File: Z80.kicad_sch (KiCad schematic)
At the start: 14 parts, among them J13 Conn_02x06_Odd_Even, J14 Conn_02x20_Odd_Even, J15 Conn_01x03_Socket, J16 Conn_01x03_Pin, SW3 RotaryEncoder_for_Coleco_20imp, U4 Z80CPU

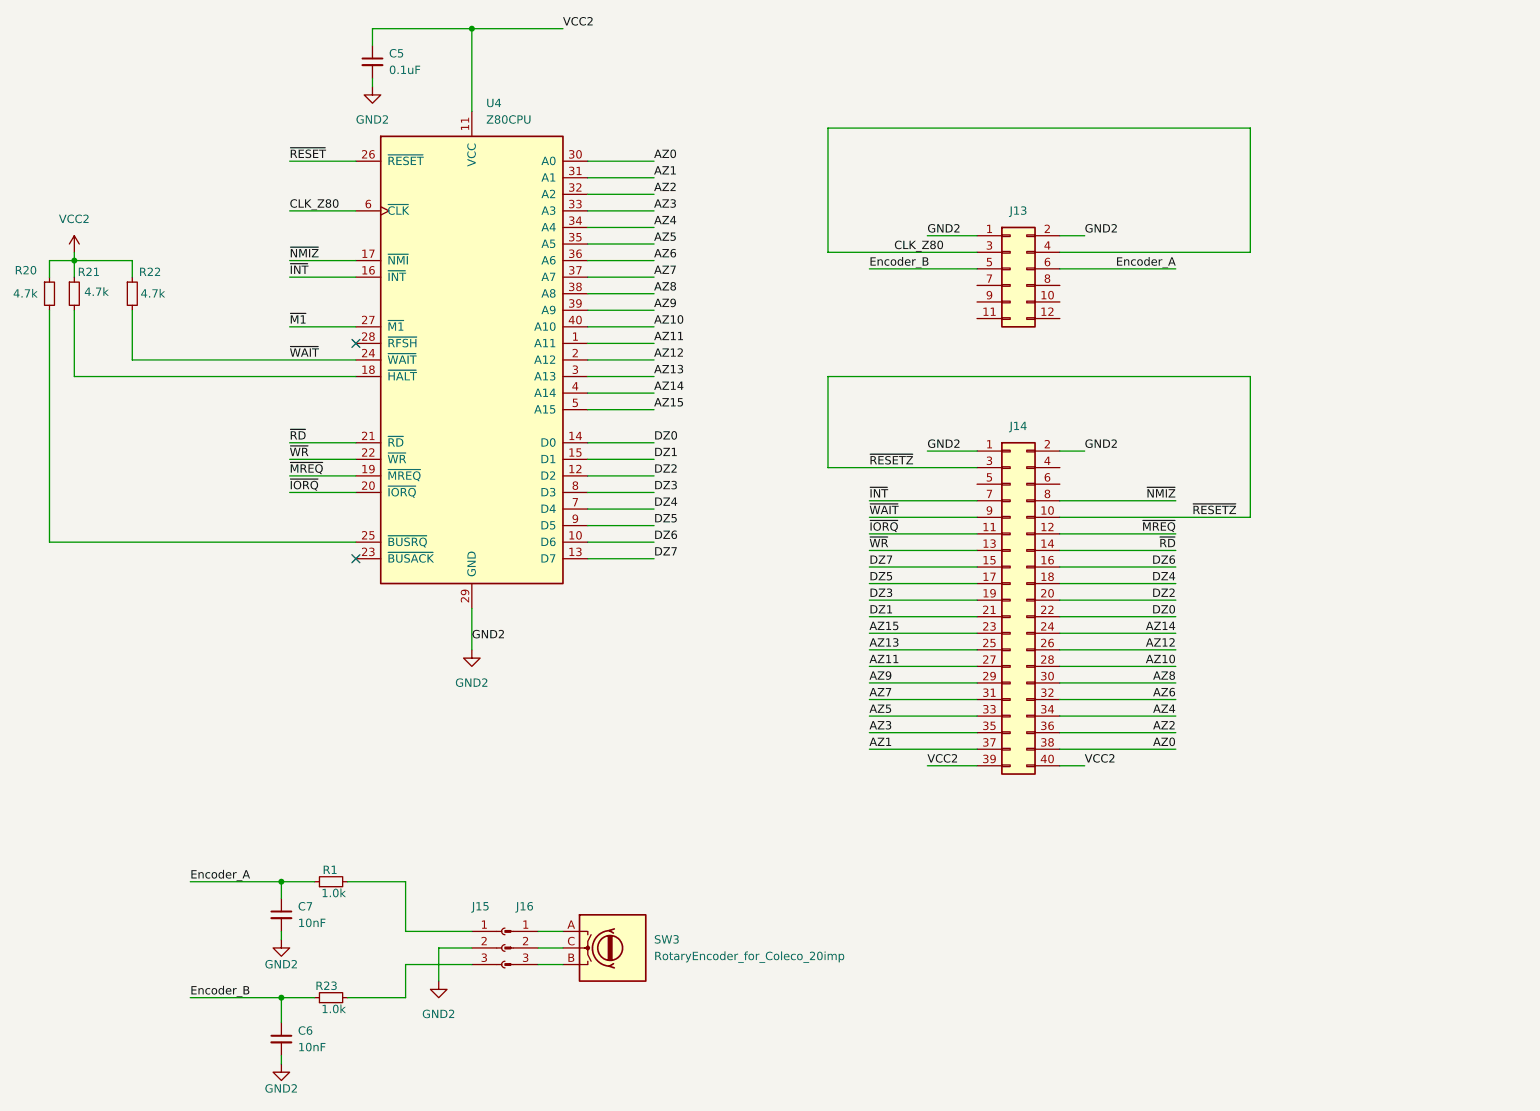
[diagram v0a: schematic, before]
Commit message: Update Z80.kicad_sch
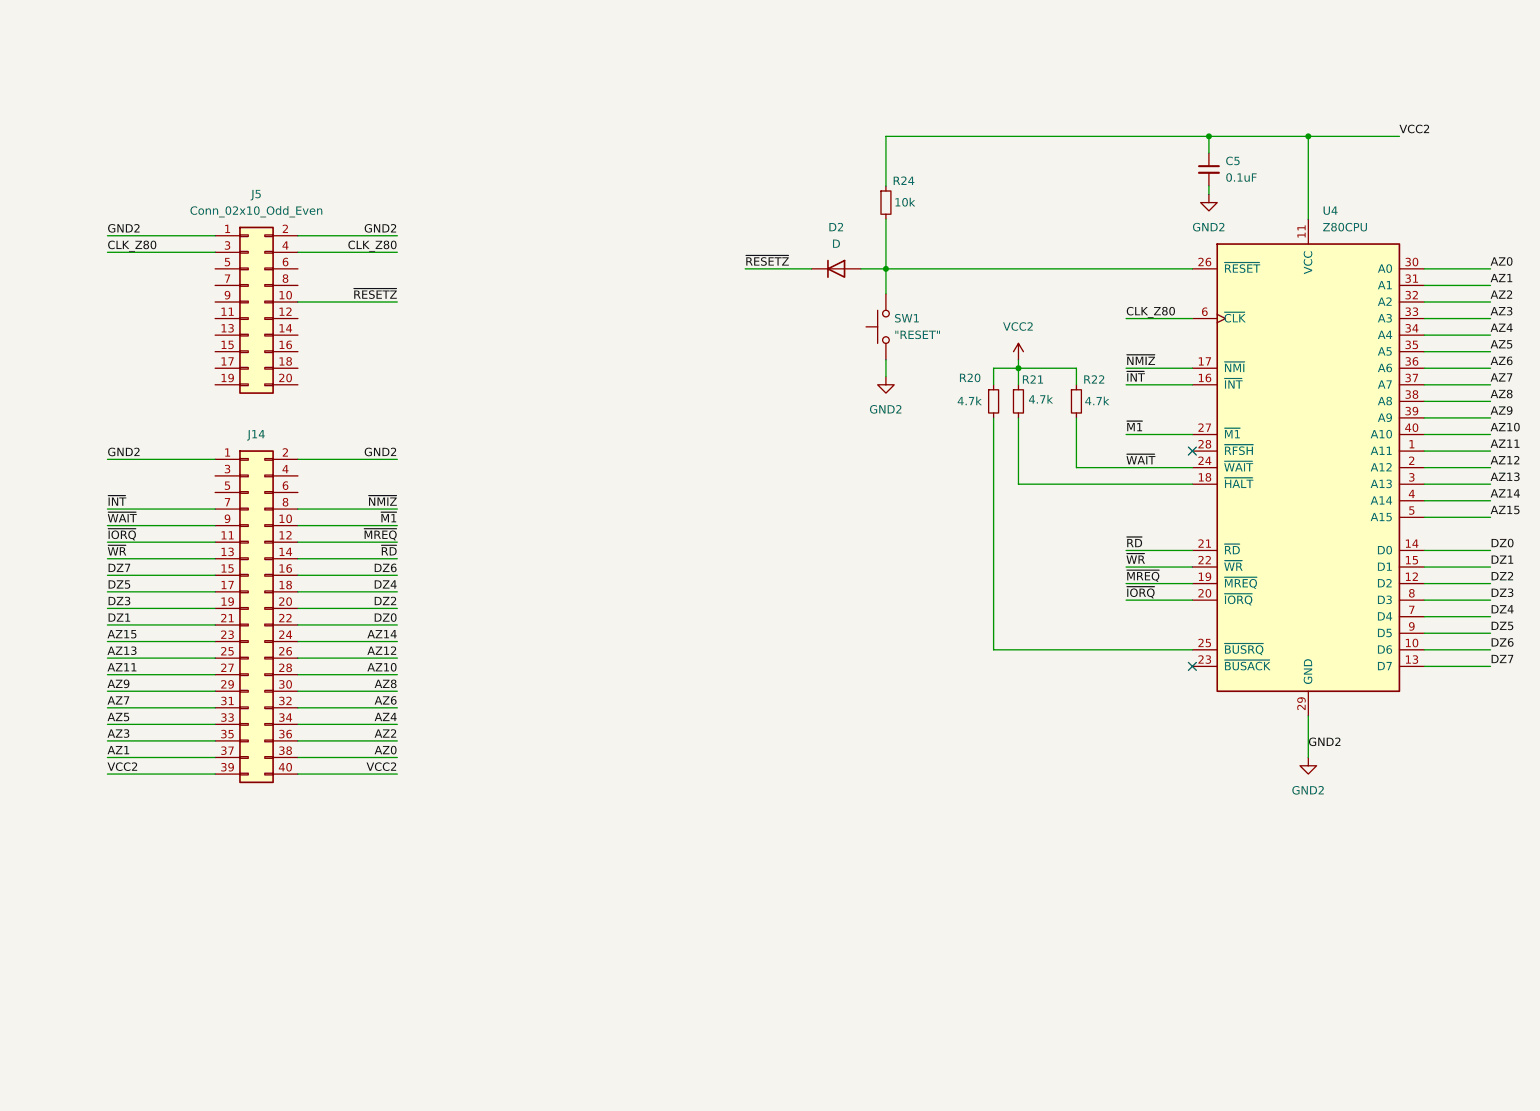
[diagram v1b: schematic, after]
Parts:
- removed C6, C7: 10nF, Capacitor_SMD:C_0805_2012Metric_Pad1.18x1.45mm_HandSolder, symbol Device:C_Small
- removed J13: Conn_02x06_Odd_Even, Z80:EDGE_2x12, symbol Connector_Generic:Conn_02x06_Odd_Even
- removed J15: Conn_01x03_Socket, symbol Connector:Conn_01x03_Socket
- removed J16: Conn_01x03_Pin, symbol Connector:Conn_01x03_Pin
- removed R1, R23: 1.0k, Resistor_SMD:R_0805_2012Metric_Pad1.20x1.40mm_HandSolder, symbol Device:R_Small
- removed SW3: RotaryEncoder_for_Coleco_20imp, symbol Device:RotaryEncoder
- added D2: D, Diode_SMD:D_1206_3216Metric_Pad1.42x1.75mm_HandSolder, symbol Device:D
- added J5: Conn_02x10_Odd_Even, Library:EDGE_2x10, symbol Connector_Generic:Conn_02x10_Odd_Even
- added R24: 10k, Resistor_SMD:R_0805_2012Metric_Pad1.20x1.40mm_HandSolder, symbol Device:R_Small
- added SW1: "RESET", Button_Switch_THT:SW_Tactile_SPST_Angled_PTS645Vx31-2LFS, symbol Switch:SW_Push
- J14: footprint Z80:EDGE_2x20 -> Library:EDGE_2x20
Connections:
- net CLK_Z80: now also J5.3 (Pin_3), J5.4 (Pin_4)
- net GND2: now also J5.1 (Pin_1), J5.2 (Pin_2), SW1.1
- net VCC2: now also R24.1
- net ~{M1}: now also J14.10 (Pin_10)
- net ~{RESETZ}: now also D2.1 (K), J5.10 (Pin_10); no longer J14.10 (Pin_10), J14.3 (Pin_3)
- net ~{RESET}: no longer names the net of U4.26 (~{RESET})
- net ~{RESET}: now also D2.2 (A), R24.2, SW1.2
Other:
- moved on the sheet: C5, J14, R20, R21, R22, U4

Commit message: Update Z80.kicad_sch
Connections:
- net ~{WAIT}: now also J5.5 (Pin_5)
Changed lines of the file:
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@@
+	(wire
+		(pts
+			(xy 36.83 69.85) (xy 36.83 109.22)
+		)
+		(stroke
+			(width 0)
+			(type default)
+		)
+	)
 	(wire
 		(pts
@@
 	(wire
 		(pts
-			(xy 48.26 109.22) (xy 64.77 109.22)
-		)
-		(stroke
-			(width 0)
-			(type default)
-		)
-	)
-	(wire
-		(pts
 			(xy 204.47 95.25) (xy 214.63 95.25)
 		)
@@
 	(wire
 		(pts
+			(xy 64.77 69.85) (xy 36.83 69.85)
+		)
+		(stroke
+			(width 0)
+			(type default)
+		)
+	)
+	(wire
+		(pts
 			(xy 167.64 62.23) (xy 167.64 69.85)
 		)
@@
 		)
 		(stroke
+			(width 0)
+			(type default)
+		)
+	)
+	(wire
+		(pts
+			(xy 36.83 109.22) (xy 64.77 109.22)
+		)
+		(stroke
